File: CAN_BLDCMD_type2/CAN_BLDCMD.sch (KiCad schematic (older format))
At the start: 213 parts, among them J1 SWD, J10 BATT_IN, J11 OUT_U, J12 OUT_V, J13 OUT_W, J14 VALVE, J15 HALL_IN, J2 CAN, J3 CAN, J4 ENC, J5 I/O0, J6 I/O1, J7 SERIAL, J8 FAN, J9 BATT_IN, Q1 MOSFET_N, Q2 MOSFET_N, Q3 MOSFET_N, Q4 MOSFET_N, Q5 MOSFET_N, Q6 MOSFET_N, Q7 NPN, Q8 NPN, SW1 SW0, SW2 SW1, SW3 RST, SW4 MODE, U1 MAX3051, U10 SI8900, U11 ADC_~RST, U12 ACS758, U13 ACS758, U14 ACS758, U15 BD9G101G, U16 LTC2644, U17 LTC2644, U18 BD33FA1, U19 LOGO, U2 BD9G101G, U20 AQM0802, U3 STM32F405RG, U4 AZ1086H, U5 ADRESS, U6 POWER_ON, U7 SI8274, U8 SI8274, U9 SI8274, Y1 8MHz

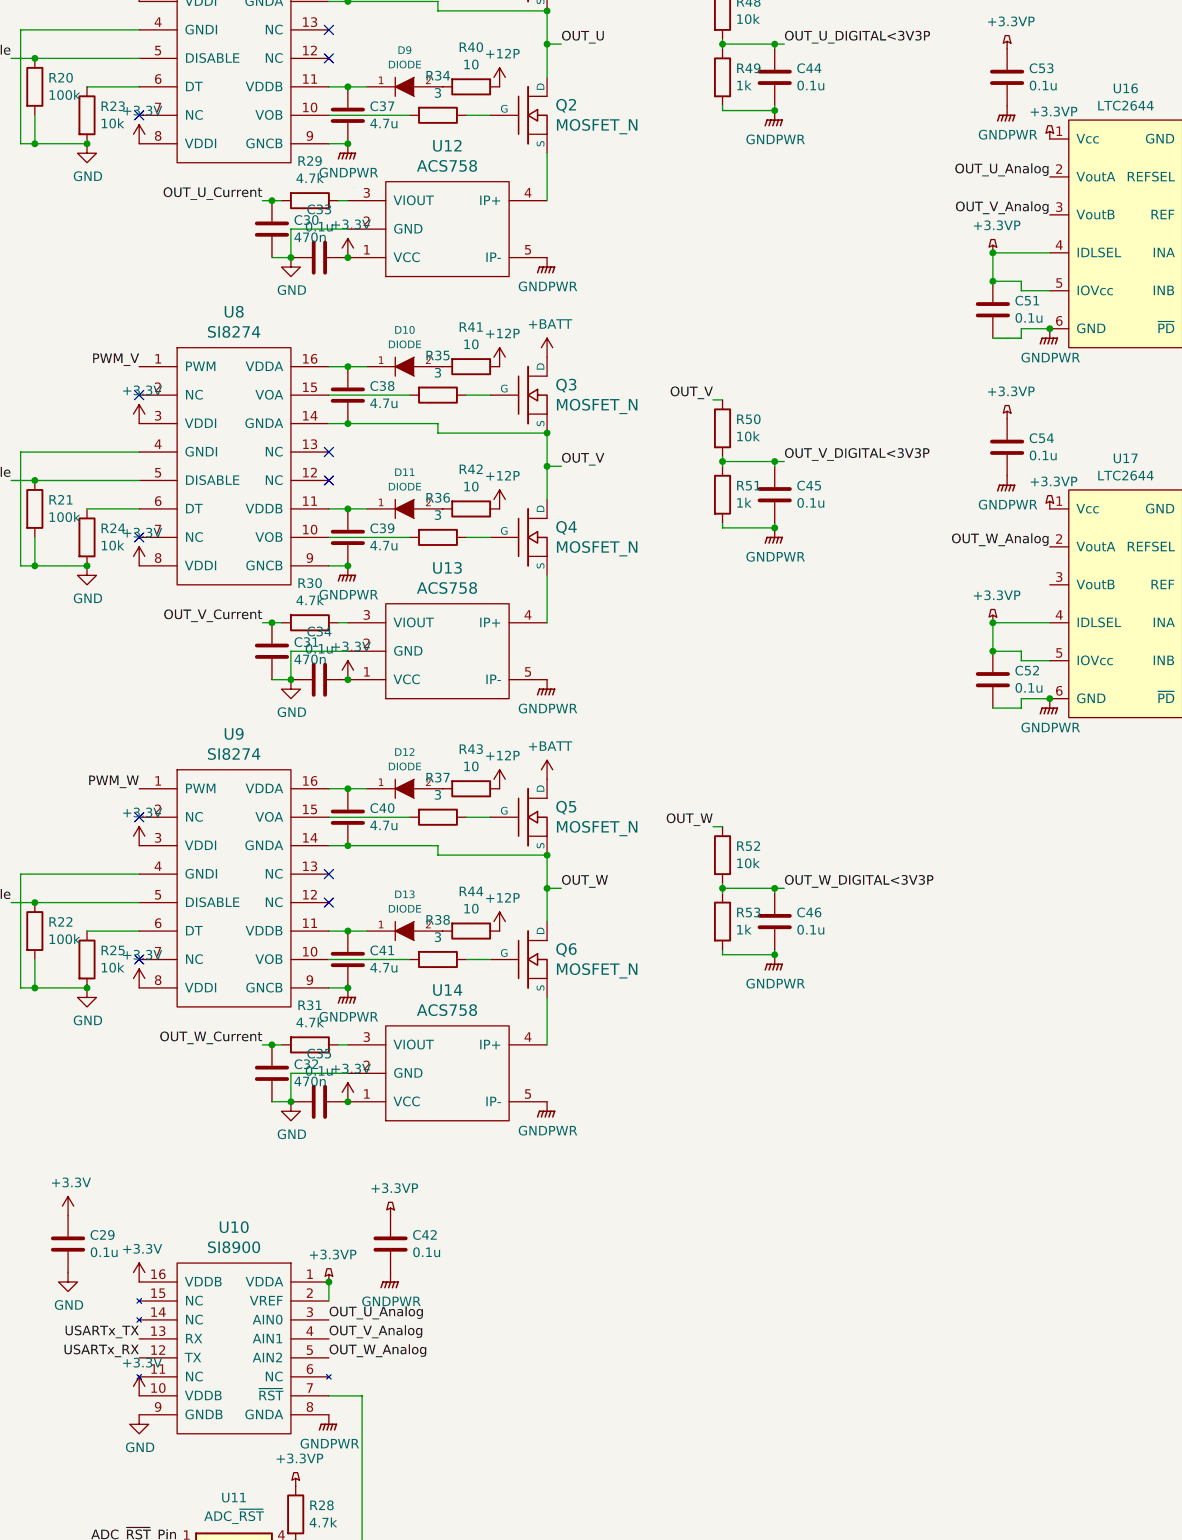
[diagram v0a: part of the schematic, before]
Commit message: MAIN基板，大体の構成完了．あとは配線を少し修正するのみ
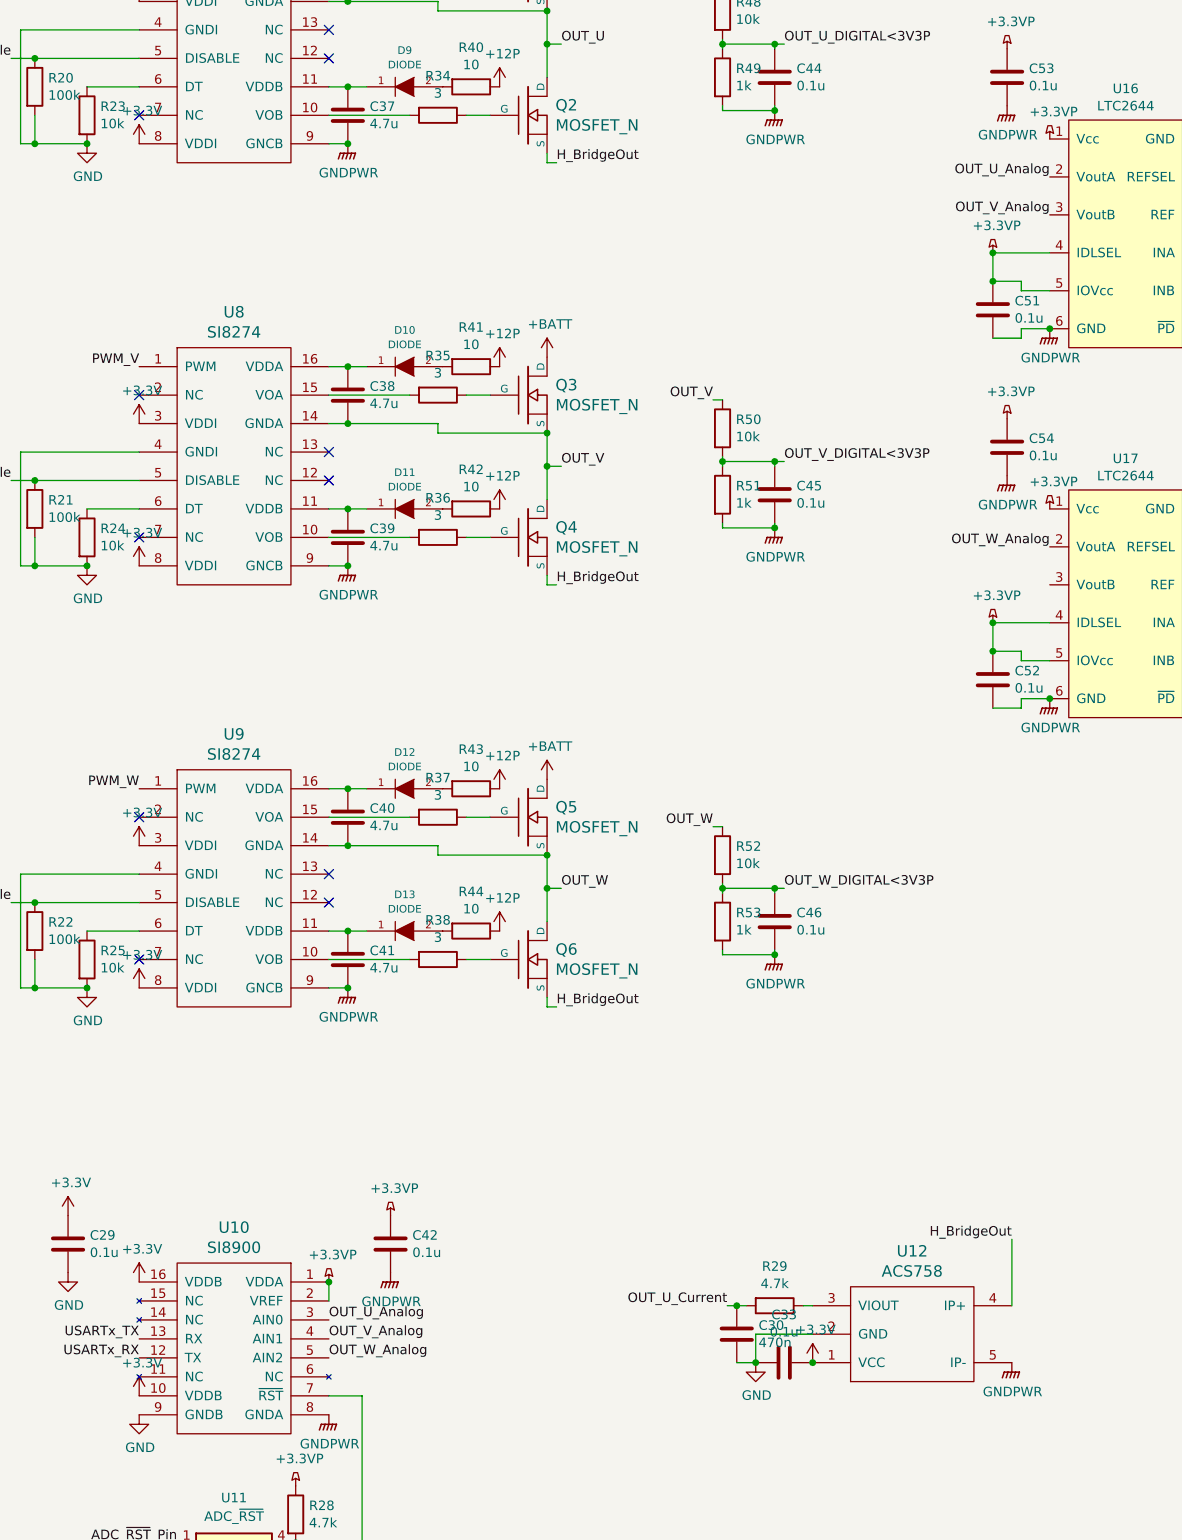
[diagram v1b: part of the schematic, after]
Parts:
- removed C31, C32: 470n, Capacitor_SMD:C_0603_1608Metric, symbol Device:C
- removed C34, C35: 0.1u, Capacitor_SMD:C_0603_1608Metric, symbol Device:C
- removed R30, R31: 4.7k, Mizz_lib:1608_WP, symbol Device:R
- removed U13, U14: ACS758, Mizz_lib:ACS785xCB, symbol Miz:ACS758
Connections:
- net H_BridgeOut: now reaches Q4.S
- net H_BridgeOut: now also Q2.S, Q6.S, U12.4 (IP+)
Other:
- moved on the sheet: C30, C33, R29, U12

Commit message: 肩痛い
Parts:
- removed C44, C45, C46, C51, C52, C53, C54: 0.1u, Capacitor_SMD:C_0603_1608Metric, symbol Device:C
- removed R51, R53: 1k, Mizz_lib:1608_WP, symbol Device:R
- removed R52: 10k, Mizz_lib:1608_WP, symbol Device:R
- removed U10: SI8900, Package_SO:SOIC-16W_7.5x10.3mm_P1.27mm, symbol Miz:SI8900
- removed U11: ADC_~RST, Package_SO:SOIC-4_4.55x2.6mm_P1.27mm, symbol Isolator:TLP291
- removed U16, U17: LTC2644, Package_SO:MSOP-12_3x4mm_P0.65mm, symbol Miz:LTC2644
- removed U18: BD33FA1, Package_TO_SOT_SMD:SOT-89-3, symbol Miz:BD33FA1
- added C31, C32, C34: 0.1u, Capacitor_SMD:C_0603_1608Metric, symbol Device:C
- added D28: LED, LED_SMD:LED_0603_1608Metric, symbol Device:LED
- added ISO1: Si8660BA, Package_SO:SOIC-16_3.9x9.9mm_P1.27mm, symbol Miz:Si866x
- added R30, R31: 100k, Mizz_lib:1608_WP, symbol Device:R
- added U10: LM324, Package_SO:TSSOP-14_4.4x5mm_P0.65mm, symbol Amplifier_Operational:LM324
- added U11: NJM78L05, Package_TO_SOT_SMD:SOT-89-3, symbol Miz:NJM78L00
- R28: value 4.7k -> 100k
- R32: value 4.7k -> 20k
- R48, R50: value 10k -> 100
- R49: value 1k -> 100
- R64: value 510 -> 1k
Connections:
- net OUT_V_DIGITAL<3V3P is gone; now on net OUT_W: R50.2
- net USARTx_RX is gone; now on net PWR_ON_Pin: U3.17 (USART2_RX/TIM5_CH4/TIM9_CH2/ADC12_IN3/TIM2_CH4/PA3)
- net +12P: now also U11.1 (Vout)
- net +3V3: now also ISO1.16 (VDD2)
- net +BATT: now also C31.2, C32.2, C34.2, U10.4 (V+)
- net ADRESS_0: now also U3.38 (PC7/TIM8_CH2/USART6_RX/TIM3_CH2); no longer U3.29 (USART3_TX/TIM2_CH3/PB10)
- net ADRESS_1: now also U3.39 (PC8/TIM8_CH3/TIM3_CH3); no longer U3.30 (USART3_RX/TIM2_CH4/PB11)
- net ADRESS_2: now also U3.40 (PC9/TIM8_CH4/TIM3_CH4); no longer U3.33 (CAN2_RX/PB12)
- net ADRESS_3: now also U3.41 (TIM1_CH1/PA8); no longer U3.34 (TIM1_CH1N/CAN2_TX/PB13)
- net GND: now also D28.1 (K), ISO1.9 (GND2); no longer R27.2
- net GNDPWR: now also ISO1.8 (GND1), U10.11 (V-), U11.2 (GND); no longer R49.2
- net I2Cx_SCL: now also U3.29 (USART3_TX/TIM2_CH3/PB10)
- net I2Cx_SDA: now also U3.30 (USART3_RX/TIM2_CH4/PB11)
- net OUT_U: now also R28.1, R48.2, U10.5 (+); no longer R48.1
- net OUT_V: now also R49.2, R30.1, U10.3 (+); no longer R50.1
- net OUT_W: now also R31.1, U10.10 (+)
- net PWR_ON_Pin: no longer U3.14 (UART4_TX/TIM2_CH1_ETR/ADC12_IN0/TIM5_CH1/PA0)
- net LED2: now reaches U3.11 (PC3/ADC12_IN13)
- net LED2: now also R27.1
- net ZERO_CROSS: now reaches R28.2
- net ZERO_CROSS: now also R30.2, R31.2, U10.2 (-), U10.6 (-), U10.9 (-)
- net +3.3VP renamed +5VP
- net +5VP: now also ISO1.1 (VDD1), U11.3 (Vin); no longer R28.1
- net ADC_~RST~_Pin renamed LOCATION_V_SIGNAL
- net LOCATION_V_SIGNAL: now also ISO1.11 (B5)
- net H_BridgeOut renamed INVERTER_OUT
- net OUT_U_Current renamed Current
- net OUT_U_DIGITAL<3V3P: no longer names the net of R49.1
- net OUT_U_DIGITAL<3V3P: now also C32.1; no longer R48.2
- net OUT_V_Current: no longer names the net of U3.26 (ADC12_IN8/TIM1_CH2N/TIM8_CH2N/TIM3_CH3/PB0)
- net OUT_W_Current: no longer names the net of U3.27 (ADC12_IN9/TIM1_CH3N/TIM8_CH3N/TIM3_CH4/PB1)
- net USARTx_TX renamed LOCATION_W_SIGNAL
- net LOCATION_W_SIGNAL: now also ISO1.12 (B4)
- new net: C31.1, R48.1
- new net: C34.1, R50.1
- new net: D28.2 (A), R27.2
- new net LOCATION_U_SIGNAL: ISO1.10 (B6), U3.14 (UART4_TX/TIM2_CH1_ETR/ADC12_IN0/TIM5_CH1/PA0)
- new net SIGNAL_U: ISO1.7 (A6), U10.7
- new net SIGNAL_V: ISO1.6 (A5), U10.1
- new net SIGNAL_W: ISO1.5 (A4), U10.8
- no-connect marks 16 -> 19
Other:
- note added: "Zero cross"
- moved on the sheet: C29, C30, C33, C42, R29, U12

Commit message: BLDC type2引き終わった，基板にミスがあった
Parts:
- added C35, C44, C45, C46: 0.1u, Mizz_lib:1608_WP, symbol Device:C
- C11, C13, C15, C16, C17, C20, C22, C23, C24, C25, C26, C27, C28, C29, C30, C5, C6, C7: footprint Capacitor_SMD:C_0603_1608Metric -> Mizz_lib:1608_WP
- D27: value 3V3P -> 5VP
- D28: value LED -> EMG
- D5: value LED -> MODE
- D6: value LED -> BUS
- R20, R21: value 100k -> 10k
- R23, R24: value 10k -> 100k
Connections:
- net +12V: now also C12.1, C14.1, D3.1 (K), U2.4 (EN), U2.5 (VCC); no longer C10.1, C9.1, D3.2 (A), J2.2 (Pin_2), J3.2 (Pin_2)
- net +3V3: now also C44.1, C45.1, C46.1
- net +BATT: now also C35.1
- net ADRESS_0: now also U3.41 (TIM1_CH1/PA8); no longer U3.38 (PC7/TIM8_CH2/USART6_RX/TIM3_CH2)
- net ADRESS_1: now also U3.40 (PC9/TIM8_CH4/TIM3_CH4); no longer U3.39 (PC8/TIM8_CH3/TIM3_CH3)
- net ADRESS_2: now also U3.45 (CAN1_TX/PA12); no longer U3.40 (PC9/TIM8_CH4/TIM3_CH4)
- net ADRESS_3: now also U3.44 (CAN1_RX/TIM1_CH4/PA11); no longer U3.41 (TIM1_CH1/PA8)
- net Drive_U_Temp: now also U3.22 (ADC12_IN6/TIM3_CH1/TIM13_CH1/PA6); no longer U3.20 (ADC12_IN4/PA4)
- net Drive_W_Temp: now also U3.20 (ADC12_IN4/PA4); no longer U3.22 (ADC12_IN6/TIM3_CH1/TIM13_CH1/PA6)
- net Enable: now also U3.16 (USART2_TX/TIM5_CH3/TIM9_CH1/ADC12_IN2/TIM2_CH3/PA2)
- net GND: now also C44.2, C45.2, C46.2
- net GNDPWR: now also C35.2
- net LOCATION_U_SIGNAL: now also U3.4 (PC15/OSC32_OUT); no longer U3.14 (UART4_TX/TIM2_CH1_ETR/ADC12_IN0/TIM5_CH1/PA0)
- net LOCATION_V_SIGNAL: now also U3.3 (PC14/OSC32_IN); no longer U3.15 (UART4_RX/ADC12_IN1/TIM5_CH2/TIM2_CH2/PA1)
- net LOCATION_W_SIGNAL: now also U3.2 (PC13); no longer U3.16 (USART2_TX/TIM5_CH3/TIM9_CH1/ADC12_IN2/TIM2_CH3/PA2)
- net PWM_U: now also U3.17 (USART2_RX/TIM5_CH4/TIM9_CH2/ADC12_IN3/TIM2_CH4/PA3)
- net PWM_V: now also U3.14 (UART4_TX/TIM2_CH1_ETR/ADC12_IN0/TIM5_CH1/PA0)
- net PWM_W: now also U3.15 (UART4_RX/ADC12_IN1/TIM5_CH2/TIM2_CH2/PA1)
- net PWR_ON_Pin: now also U3.58 (TIM4_CH1/CAN2_TX/USART1_TX/PB6); no longer U3.17 (USART2_RX/TIM5_CH4/TIM9_CH2/ADC12_IN3/TIM2_CH4/PA3)
- net SW0: now also U3.54 (PD2/UART5_RX); no longer U3.2 (PC13)
- net SW1: now also U3.55 (TIM2_CH2/PB3); no longer U3.3 (PC14/OSC32_IN)
- net SW_MODE: now also U3.59 (USART1_RX/TIM4_CH2/PB7); no longer U3.37 (PC6/TIM8_CH1/USART6_TX/TIM3_CH1)
- net VALVE_0: now also U3.26 (ADC12_IN8/TIM1_CH2N/TIM8_CH2N/TIM3_CH3/PB0)
- net VALVE_1: now also U3.27 (ADC12_IN9/TIM1_CH3N/TIM8_CH3N/TIM3_CH4/PB1)
- new net CAN_Vdd: C10.1, C9.1, D3.2 (A), J2.2 (Pin_2), J3.2 (Pin_2)
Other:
- note added: "TIM2"
- moved on the sheet: D28, D6, R14, R27, R28, R30, R31, U10A, U10B, U10C, U10D, U10E

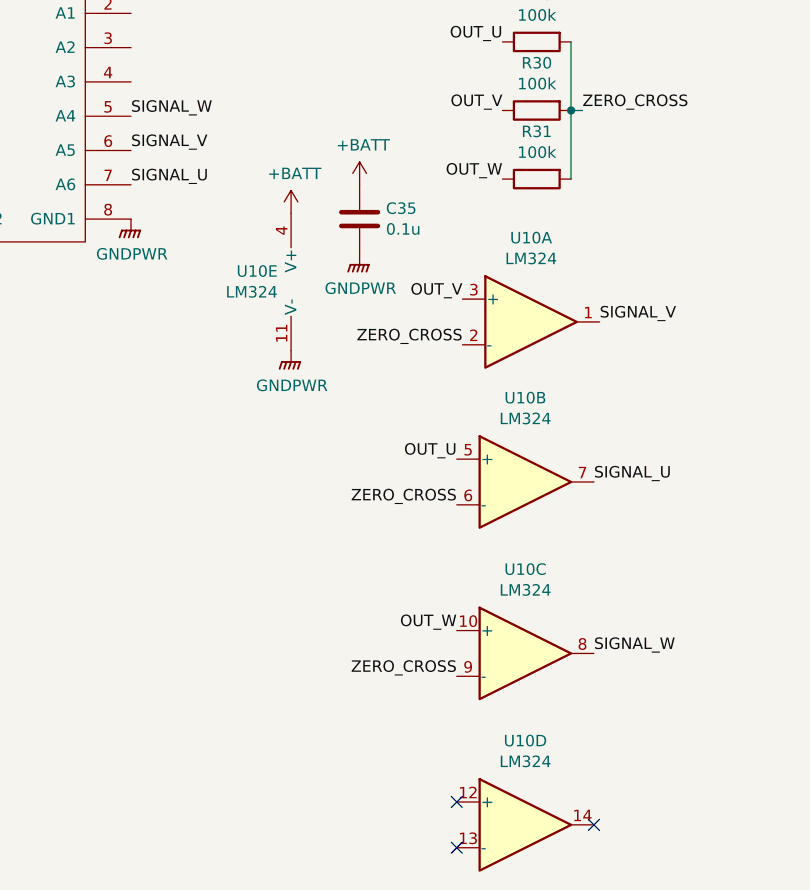
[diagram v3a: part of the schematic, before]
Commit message: BLDCMD type2,ロータ位置推定回路修正
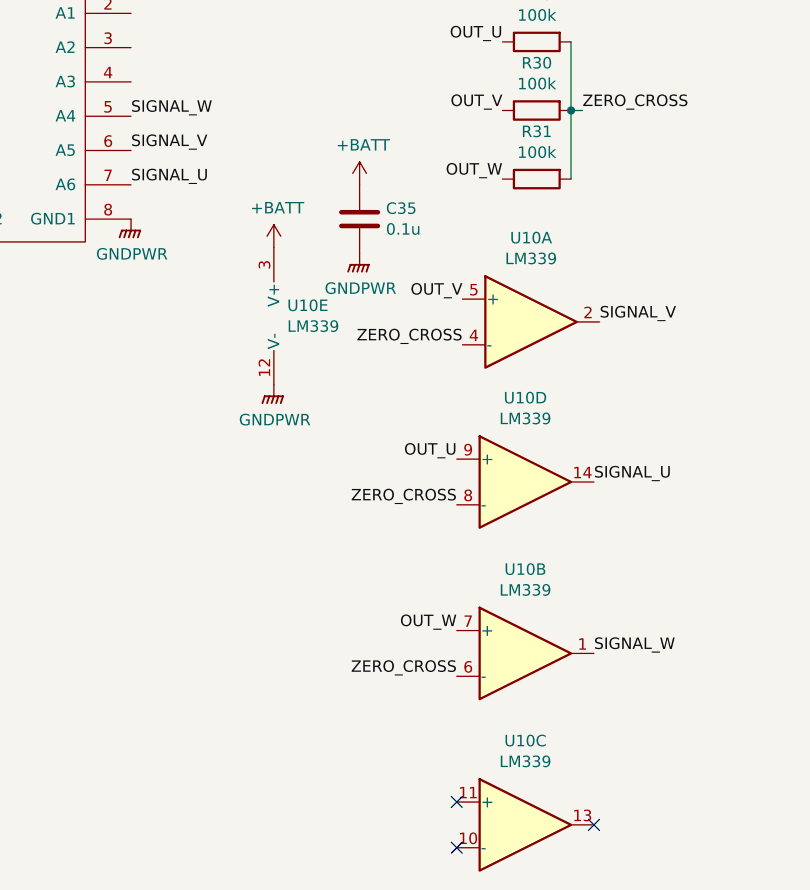
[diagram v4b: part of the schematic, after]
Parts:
- removed U10: LM324, Package_SO:TSSOP-14_4.4x5mm_P0.65mm, symbol Amplifier_Operational:LM324
- added U10: LM339, Package_SO:SOIC-14_3.9x8.7mm_P1.27mm, symbol Comparator:LM339
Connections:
- net +BATT: now also U10.3 (V+)
- net GNDPWR: now also U10.12 (V-)
- net OUT_U: now also U10.9 (+)
- net OUT_V: now also U10.5 (+)
- net OUT_W: now also U10.7 (+)
- net SIGNAL_U: now also U10.14
- net SIGNAL_V: now also U10.2
- net SIGNAL_W: now also U10.1
- net ZERO_CROSS: now also U10.4 (-), U10.6 (-), U10.8 (-)
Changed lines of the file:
@@
 	1    0    0    -1
-$EndComp
-$Comp
-L Amplifier_Operational:LM324 U10
-U 2 1 5E98191C
-P 17650 13825
-F 0 "U10" H 17650 14192 50  0000 C CNN
-F 1 "LM324" H 17650 14101 50  0000 C CNN
-F 2 "Package_SO:TSSOP-14_4.4x5mm_P0.65mm" H 17600 13925 50  0001 C CNN
-F 3 "http://www.ti.com/lit/ds/symlink/lm2902-n.pdf" H 17700 14025 50  0001 C CNN
-	2    17650 13825
-	1    0    0    -1
-$EndComp
-$Comp
-L Amplifier_Operational:LM324 U10
-U 3 1 5E983F59
-P 17650 14575
-F 0 "U10" H 17650 14942 50  0000 C CNN
-F 1 "LM324" H 17650 14851 50  0000 C CNN
-F 2 "Package_SO:TSSOP-14_4.4x5mm_P0.65mm" H 17600 14675 50  0001 C CNN
-F 3 "http://www.ti.com/lit/ds/symlink/lm2902-n.pdf" H 17700 14775 50  0001 C CNN
-	3    17650 14575
-	1    0    0    -1
-$EndComp
-$Comp
-L Amplifier_Operational:LM324 U10
-U 4 1 5E98679B
-P 17650 15325
-F 0 "U10" H 17650 15692 50  0000 C CNN
-F 1 "LM324" H 17650 15601 50  0000 C CNN
-F 2 "Package_SO:TSSOP-14_4.4x5mm_P0.65mm" H 17600 15425 50  0001 C CNN
-F 3 "http://www.ti.com/lit/ds/symlink/lm2902-n.pdf" H 17700 15525 50  0001 C CNN
-	4    17650 15325
-	1    0    0    -1
-$EndComp
-$Comp
-L Amplifier_Operational:LM324 U10
-U 5 1 5E9B09F3
-P 16525 12950
-F 0 "U10" H 16483 12996 50  0000 L CNN
-F 1 "LM324" H 16483 12905 50  0000 L CNN
-F 2 "Package_SO:TSSOP-14_4.4x5mm_P0.65mm" H 16475 13050 50  0001 C CNN
-F 3 "http://www.ti.com/lit/ds/symlink/lm2902-n.pdf" H 16575 13150 50  0001 C CNN
-	5    16525 12950
-	-1   0    0    -1
 $EndComp
 Text Label 17375 13025 2    50   ~ 0
@@
 OUT_U
 $Comp
-L Amplifier_Operational:LM324 U10
-U 1 1 5E97F1B3
-P 17675 13125
-F 0 "U10" H 17675 13492 50  0000 C CNN
-F 1 "LM324" H 17675 13401 50  0000 C CNN
-F 2 "Package_SO:TSSOP-14_4.4x5mm_P0.65mm" H 17625 13225 50  0001 C CNN
-F 3 "http://www.ti.com/lit/ds/symlink/lm2902-n.pdf" H 17725 13325 50  0001 C CNN
-	1    17675 13125
-	1    0    0    -1
-$EndComp
-$Comp
 L power:GNDPWR #PWR0159
 U 1 1 5EADFA37
-P 16625 13250
-F 0 "#PWR0159" H 16625 13050 50  0001 C CNN
-F 1 "GNDPWR" H 16629 13096 50  0000 C CNN
-F 2 "" H 16625 13200 50  0001 C CNN
-F 3 "" H 16625 13200 50  0001 C CNN
-	1    16625 13250
+P 16550 13400
+F 0 "#PWR0159" H 16550 13200 50  0001 C CNN
+F 1 "GNDPWR" H 16554 13246 50  0000 C CNN
+F 2 "" H 16550 13350 50  0001 C CNN
+F 3 "" H 16550 13350 50  0001 C CNN
+	1    16550 13400
 	1    0    0    -1
 $EndComp
@@
 L power:+BATT #PWR0173
 U 1 1 5E75E346
-P 16625 12650
-F 0 "#PWR0173" H 16625 12500 50  0001 C CNN
-F 1 "+BATT" H 16640 12823 50  0000 C CNN
-F 2 "" H 16625 12650 50  0001 C CNN
-F 3 "" H 16625 12650 50  0001 C CNN
-	1    16625 12650
+P 16550 12800
+F 0 "#PWR0173" H 16550 12650 50  0001 C CNN
+F 1 "+BATT" H 16565 12973 50  0000 C CNN
+F 2 "" H 16550 12800 50  0001 C CNN
+F 3 "" H 16550 12800 50  0001 C CNN
+	1    16550 12800
 	1    0    0    -1
 $EndComp
@@
 	1    0    0    -1
 $EndComp
+$Comp
+L Comparator:LM339 U10
+U 1 1 5E976A29
+P 17675 13125
+F 0 "U10" H 17675 13492 50  0000 C CNN
+F 1 "LM339" H 17675 13401 50  0000 C CNN
+F 2 "Package_SO:SOIC-14_3.9x8.7mm_P1.27mm" H 17625 13225 50  0001 C CNN
+F 3 "https://www.st.com/resource/en/datasheet/lm139.pdf" H 17725 13325 50  0001 C CNN
+	1    17675 13125
+	1    0    0    -1
+$EndComp
+$Comp
+L Comparator:LM339 U10
+U 2 1 5E97CA91
+P 17650 14575
+F 0 "U10" H 17650 14942 50  0000 C CNN
+F 1 "LM339" H 17650 14851 50  0000 C CNN
+F 2 "Package_SO:SOIC-14_3.9x8.7mm_P1.27mm" H 17600 14675 50  0001 C CNN
+F 3 "https://www.st.com/resource/en/datasheet/lm139.pdf" H 17700 14775 50  0001 C CNN
+	2    17650 14575
+	1    0    0    -1
+$EndComp
+$Comp
+L Comparator:LM339 U10
+U 3 1 5E97E779
+P 17650 15325
+F 0 "U10" H 17650 15692 50  0000 C CNN
+F 1 "LM339" H 17650 15601 50  0000 C CNN
+F 2 "Package_SO:SOIC-14_3.9x8.7mm_P1.27mm" H 17600 15425 50  0001 C CNN
+F 3 "https://www.st.com/resource/en/datasheet/lm139.pdf" H 17700 15525 50  0001 C CNN
+	3    17650 15325
+	1    0    0    -1
+$EndComp
+$Comp
+L Comparator:LM339 U10
+U 4 1 5E985454
+P 17650 13825
+F 0 "U10" H 17650 14192 50  0000 C CNN
+F 1 "LM339" H 17650 14101 50  0000 C CNN
+F 2 "Package_SO:SOIC-14_3.9x8.7mm_P1.27mm" H 17600 13925 50  0001 C CNN
+F 3 "https://www.st.com/resource/en/datasheet/lm139.pdf" H 17700 14025 50  0001 C CNN
+	4    17650 13825
+	1    0    0    -1
+$EndComp
+$Comp
+L Comparator:LM339 U10
+U 5 1 5E986BCB
+P 16650 13100
+F 0 "U10" H 16608 13146 50  0000 L CNN
+F 1 "LM339" H 16608 13055 50  0000 L CNN
+F 2 "Package_SO:SOIC-14_3.9x8.7mm_P1.27mm" H 16600 13200 50  0001 C CNN
+F 3 "https://www.st.com/resource/en/datasheet/lm139.pdf" H 16700 13300 50  0001 C CNN
+	5    16650 13100
+	1    0    0    -1
+$EndComp
